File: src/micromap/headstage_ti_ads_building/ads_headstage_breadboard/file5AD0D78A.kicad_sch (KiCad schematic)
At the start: 21 parts

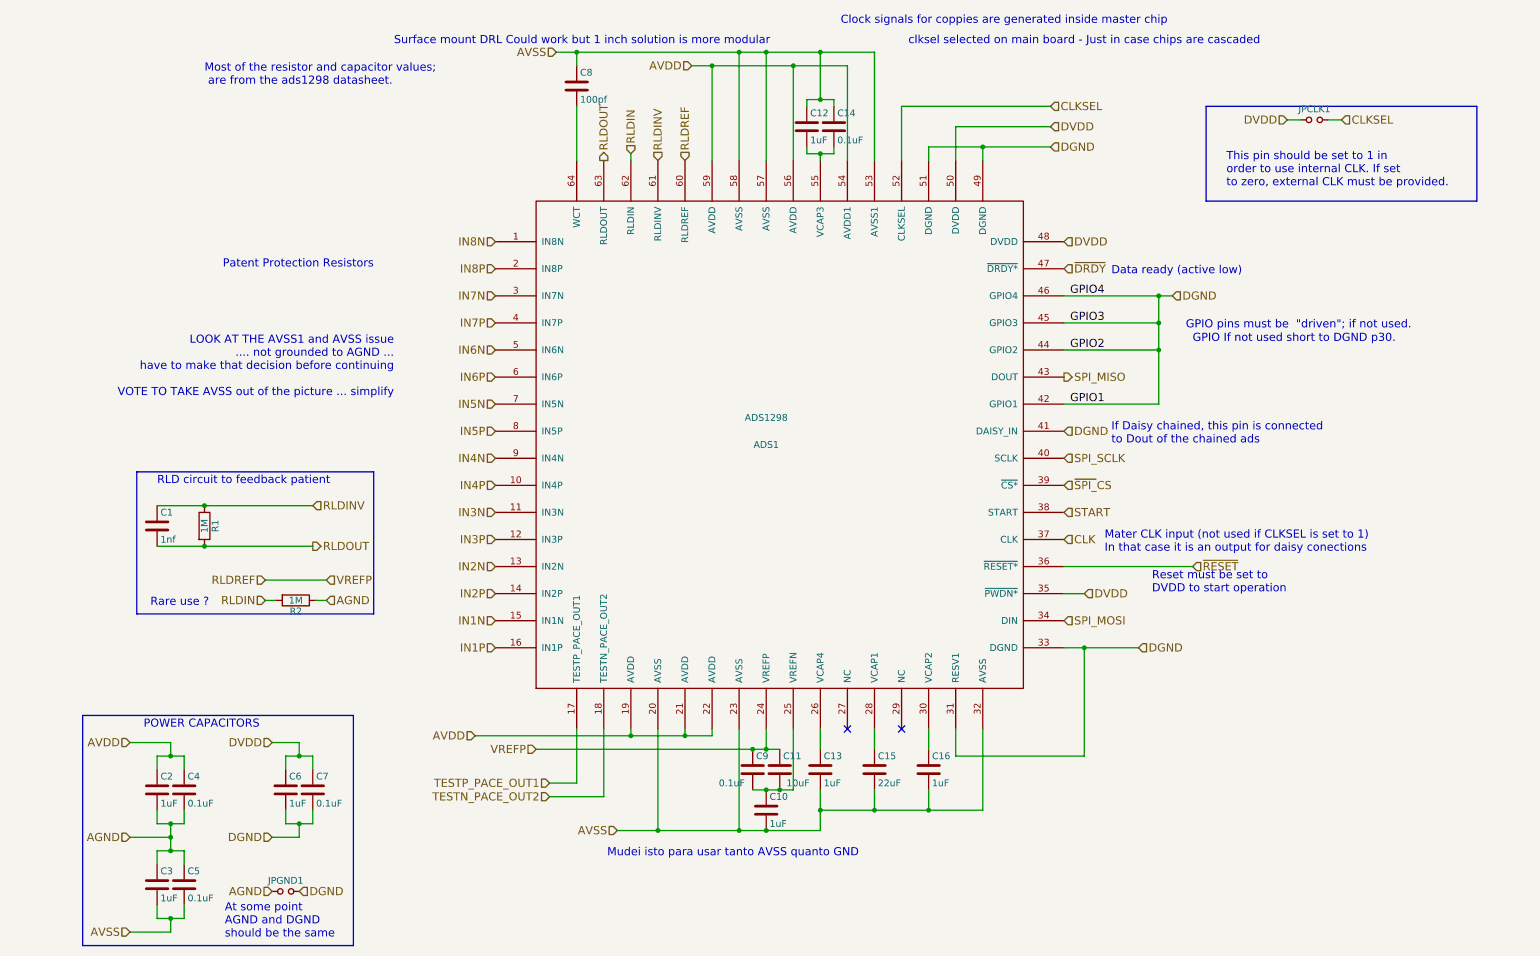
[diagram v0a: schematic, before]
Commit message: Updates on ads functions and square
- Clean data
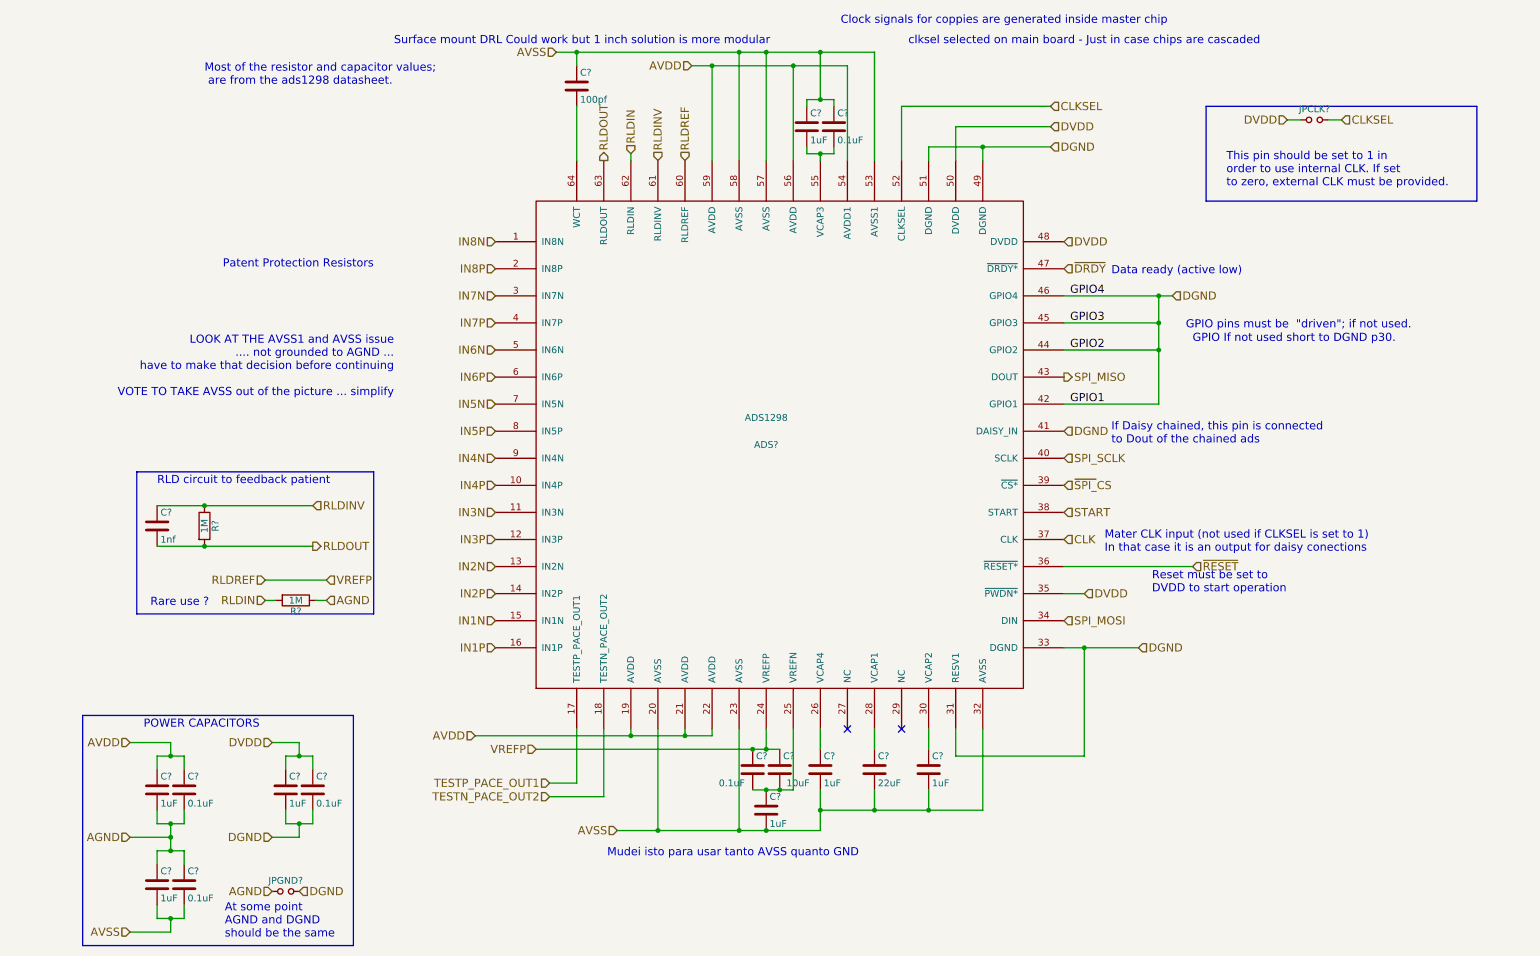
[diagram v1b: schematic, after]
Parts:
- renumbered ADS1 to ADS?, C1 to C?, C15 to C?, C16 to C?, C11 to C?, C9 to C?, C13 to C?, C4 to C?, C2 to C?, C5 to C?, C3 to C?, C7 to C?, C6 to C?, C14 to C?, C12 to C?, C8 to C?, C10 to C?, JPCLK1 to JPCLK?, JPGND1 to JPGND?, R1 to R?, R2 to R?
